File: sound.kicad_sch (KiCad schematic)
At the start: 19 parts, among them IC1 MAX4466EXK+T, U202 LSM6DS3

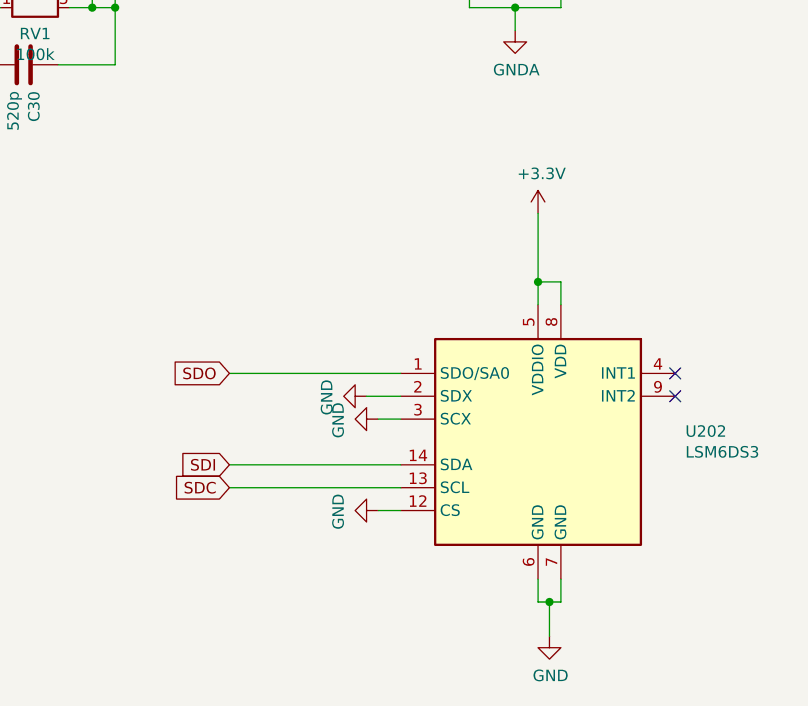
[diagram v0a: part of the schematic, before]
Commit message: Updated PCB after DRC. Updated Connector lib.
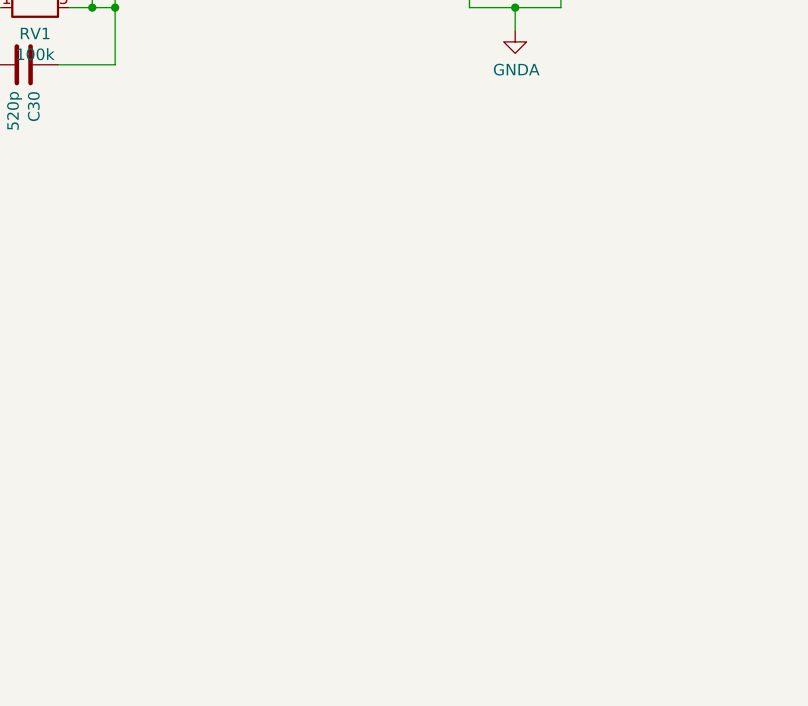
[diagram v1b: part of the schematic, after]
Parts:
- removed U202: LSM6DS3, Package_LGA:LGA-14_3x2.5mm_P0.5mm_LayoutBorder3x4y, symbol Sensor_Motion:LSM6DS3
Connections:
- no-connect marks 2 -> 0
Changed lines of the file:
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@@
   (junction (at 170.18 52.07) (diameter 0) (color 0 0 0 0)
   )
-  (junction (at 167.64 97.79) (diameter 0) (color 0 0 0 0)
-  )
   (junction (at 48.26 52.07) (diameter 0) (color 0 0 0 0)
   )
@@
   (junction (at 48.26 39.37) (diameter 0) (color 0 0 0 0)
   )
-  (junction (at 168.91 133.35) (diameter 0) (color 0 0 0 0)
-  )
   (junction (at 160.02 52.07) (diameter 0) (color 0 0 0 0)
   )
@@
   (junction (at 78.74 52.07) (diameter 0) (color 0 0 0 0)
   )
-  (no_connect (at 182.88 107.95))
-  (no_connect (at 182.88 110.49))
   (wire (pts (xy 111.76 63.5) (xy 118.11 63.5))
     (stroke (width 0) (type default) (color 0 0 0 0))
@@
     (stroke (width 0) (type default) (color 0 0 0 0))
   )
-  (wire (pts (xy 167.64 133.35) (xy 167.64 130.81))
-    (stroke (width 0) (type default) (color 0 0 0 0))
-  )
   (wire (pts (xy 88.9 57.15) (xy 88.9 67.31))
     (stroke (width 0) (type default) (color 0 0 0 0))
@@
     (stroke (width 0) (type default) (color 0 0 0 0))
   )
-  (wire (pts (xy 149.86 113.03) (xy 152.4 113.03))
-    (stroke (width 0) (type default) (color 0 0 0 0))
-  )
   (wire (pts (xy 120.65 52.07) (xy 120.65 67.31))
     (stroke (width 0) (type default) (color 0 0 0 0))
@@
     (stroke (width 0) (type default) (color 0 0 0 0))
   )
-  (wire (pts (xy 168.91 133.35) (xy 167.64 133.35))
-    (stroke (width 0) (type default) (color 0 0 0 0))
-  )
-  (wire (pts (xy 168.91 137.16) (xy 168.91 133.35))
-    (stroke (width 0) (type default) (color 0 0 0 0))
-  )
   (wire (pts (xy 78.74 50.8) (xy 78.74 52.07))
     (stroke (width 0) (type default) (color 0 0 0 0))
   )
-  (wire (pts (xy 133.35 120.65) (xy 152.4 120.65))
-    (stroke (width 0) (type default) (color 0 0 0 0))
-  )
   (wire (pts (xy 48.26 52.07) (xy 64.77 52.07))
     (stroke (width 0) (type default) (color 0 0 0 0))
@@
     (stroke (width 0) (type default) (color 0 0 0 0))
   )
-  (wire (pts (xy 170.18 97.79) (xy 167.64 97.79))
-    (stroke (width 0) (type default) (color 0 0 0 0))
-  )
   (wire (pts (xy 88.9 73.66) (xy 88.9 77.47))
     (stroke (width 0) (type default) (color 0 0 0 0))
@@
     (stroke (width 0) (type default) (color 0 0 0 0))
   )
-  (wire (pts (xy 170.18 100.33) (xy 170.18 97.79))
-    (stroke (width 0) (type default) (color 0 0 0 0))
-  )
-  (wire (pts (xy 167.64 90.17) (xy 167.64 97.79))
-    (stroke (width 0) (type default) (color 0 0 0 0))
-  )
   (wire (pts (xy 139.7 60.96) (xy 147.32 60.96))
     (stroke (width 0) (type default) (color 0 0 0 0))
@@
     (stroke (width 0) (type default) (color 0 0 0 0))
   )
-  (wire (pts (xy 149.86 123.19) (xy 152.4 123.19))
-    (stroke (width 0) (type default) (color 0 0 0 0))
-  )
   (wire (pts (xy 170.18 55.88) (xy 170.18 52.07))
     (stroke (width 0) (type default) (color 0 0 0 0))
@@
     (stroke (width 0) (type default) (color 0 0 0 0))
   )
-  (wire (pts (xy 167.64 97.79) (xy 167.64 100.33))
-    (stroke (width 0) (type default) (color 0 0 0 0))
-  )
   (wire (pts (xy 114.3 73.66) (xy 120.65 73.66))
     (stroke (width 0) (type default) (color 0 0 0 0))
@@
     (stroke (width 0) (type default) (color 0 0 0 0))
   )
-  (wire (pts (xy 133.35 118.11) (xy 152.4 118.11))
-    (stroke (width 0) (type default) (color 0 0 0 0))
-  )
   (wire (pts (xy 78.74 43.18) (xy 78.74 40.64))
     (stroke (width 0) (type default) (color 0 0 0 0))
@@
     (stroke (width 0) (type default) (color 0 0 0 0))
   )
-  (wire (pts (xy 170.18 133.35) (xy 168.91 133.35))
-    (stroke (width 0) (type default) (color 0 0 0 0))
-  )
   (wire (pts (xy 165.1 69.85) (xy 165.1 67.31))
     (stroke (width 0) (type default) (color 0 0 0 0))
@@
     (stroke (width 0) (type default) (color 0 0 0 0))
   )
-  (wire (pts (xy 148.59 110.49) (xy 152.4 110.49))
-    (stroke (width 0) (type default) (color 0 0 0 0))
-  )
   (wire (pts (xy 72.39 52.07) (xy 78.74 52.07))
     (stroke (width 0) (type default) (color 0 0 0 0))
@@
     (stroke (width 0) (type default) (color 0 0 0 0))
   )
-  (wire (pts (xy 133.35 107.95) (xy 152.4 107.95))
-    (stroke (width 0) (type default) (color 0 0 0 0))
-  )
   (wire (pts (xy 88.9 97.79) (xy 88.9 95.25))
     (stroke (width 0) (type default) (color 0 0 0 0))
@@
   )
   (wire (pts (xy 170.18 67.31) (xy 170.18 63.5))
-    (stroke (width 0) (type default) (color 0 0 0 0))
-  )
-  (wire (pts (xy 170.18 130.81) (xy 170.18 133.35))
     (stroke (width 0) (type default) (color 0 0 0 0))
   )
@@
   (label "AUDIO_AMP-" (at 88.9 71.12 0)
     (effects (font (size 1.27 1.27)) (justify left bottom))
-  )
-  (global_label "SDO" (shape input) (at 133.35 107.95 180) (fields_autoplaced)
-    (effects (font (size 1.27 1.27)) (justify right))
-    (property "Intersheet References" "${INTERSHEET_REFS}" (id 0) (at 0 0 0)
-      (effects (font (size 1.27 1.27)) hide)
-    )
-  )
-  (global_label "SDI" (shape input) (at 133.35 118.11 180) (fields_autoplaced)
-    (effects (font (size 1.27 1.27)) (justify right))
-    (property "Intersheet References" "${INTERSHEET_REFS}" (id 0) (at 0 0 0)
-      (effects (font (size 1.27 1.27)) hide)
-    )
-  )
-  (global_label "SDC" (shape input) (at 133.35 120.65 180) (fields_autoplaced)
-    (effects (font (size 1.27 1.27)) (justify right))
-    (property "Intersheet References" "${INTERSHEET_REFS}" (id 0) (at 0 0 0)
-      (effects (font (size 1.27 1.27)) hide)
-    )
   )
   (global_label "AUDIO_OUT" (shape input) (at 180.34 50.8 0) (fields_autoplaced)
@@
       (effects (font (size 1.27 1.27)) hide)
     )
-    (pin "1")
-  )
-  (symbol (lib_id "Sensor_Motion:LSM6DS3") (at 167.64 115.57 0) (unit 1)
-    (in_bom yes) (on_board yes)
-    (property "Reference" "U202" (id 0) (at 183.9976 114.4016 0)
-      (effects (font (size 1.27 1.27)) (justify left))
-    )
-    (property "Value" "LSM6DS3" (id 1) (at 183.9976 116.713 0)
-      (effects (font (size 1.27 1.27)) (justify left))
-    )
-    (property "Footprint" "Package_LGA:LGA-14_3x2.5mm_P0.5mm_LayoutBorder3x4y" (id 2) (at 157.48 133.35 0)
-      (effects (font (size 1.27 1.27)) (justify left) hide)
-    )
-    (property "Datasheet" "www.st.com/resource/en/datasheet/lsm6ds3.pdf" (id 3) (at 170.18 132.08 0)
-      (effects (font (size 1.27 1.27)) hide)
-    )
-    (pin "1")
-    (pin "10")
-    (pin "11")
-    (pin "12")
-    (pin "13")
-    (pin "14")
-    (pin "2")
-    (pin "3")
-    (pin "4")
-    (pin "5")
-    (pin "6")
-    (pin "7")
-    (pin "8")
-    (pin "9")
-  )
-  (symbol (lib_id "power:GND") (at 168.91 137.16 0) (unit 1)
-    (in_bom yes) (on_board yes)
-    (property "Reference" "#PWR0124" (id 0) (at 168.91 143.51 0)
-      (effects (font (size 1.27 1.27)) hide)
-    )
-    (property "Value" "GND" (id 1) (at 169.037 141.5542 0))
-    (property "Footprint" "" (id 2) (at 168.91 137.16 0)
-      (effects (font (size 1.27 1.27)) hide)
-    )
-    (property "Datasheet" "" (id 3) (at 168.91 137.16 0)
-      (effects (font (size 1.27 1.27)) hide)
-    )
-    (pin "1")
-  )
-  (symbol (lib_id "power:+3.3V") (at 167.64 90.17 0) (unit 1)
-    (in_bom yes) (on_board yes)
-    (property "Reference" "#PWR0125" (id 0) (at 167.64 93.98 0)
-      (effects (font (size 1.27 1.27)) hide)
-    )
-    (property "Value" "+3.3V" (id 1) (at 168.021 85.7758 0))
-    (property "Footprint" "" (id 2) (at 167.64 90.17 0)
-      (effects (font (size 1.27 1.27)) hide)
-    )
-    (property "Datasheet" "" (id 3) (at 167.64 90.17 0)
-      (effects (font (size 1.27 1.27)) hide)
-    )
-    (pin "1")
-  )
-  (symbol (lib_id "power:GND") (at 149.86 113.03 270) (unit 1)
-    (in_bom yes) (on_board yes)
-    (property "Reference" "#PWR0126" (id 0) (at 143.51 113.03 0)
-      (effects (font (size 1.27 1.27)) hide)
-    )
-    (property "Value" "GND" (id 1) (at 145.4658 113.157 0))
-    (property "Footprint" "" (id 2) (at 149.86 113.03 0)
-      (effects (font (size 1.27 1.27)) hide)
-    )
-    (property "Datasheet" "" (id 3) (at 149.86 113.03 0)
-      (effects (font (size 1.27 1.27)) hide)
-    )
-    (pin "1")
-  )
-  (symbol (lib_id "power:GND") (at 148.59 110.49 270) (unit 1)
-    (in_bom yes) (on_board yes)
-    (property "Reference" "#PWR0127" (id 0) (at 142.24 110.49 0)
-      (effects (font (size 1.27 1.27)) hide)
-    )
-    (property "Value" "GND" (id 1) (at 144.1958 110.617 0))
-    (property "Footprint" "" (id 2) (at 148.59 110.49 0)
-      (effects (font (size 1.27 1.27)) hide)
-    )
-    (property "Datasheet" "" (id 3) (at 148.59 110.49 0)
-      (effects (font (size 1.27 1.27)) hide)
-    )
-    (pin "1")
-  )
-  (symbol (lib_id "power:GND") (at 149.86 123.19 270) (unit 1)
-    (in_bom yes) (on_board yes)
-    (property "Reference" "#PWR0128" (id 0) (at 143.51 123.19 0)
-      (effects (font (size 1.27 1.27)) hide)
-    )
-    (property "Value" "GND" (id 1) (at 145.4658 123.317 0))
-    (property "Footprint" "" (id 2) (at 149.86 123.19 0)
-      (effects (font (size 1.27 1.27)) hide)
-    )
-    (property "Datasheet" "" (id 3) (at 149.86 123.19 0)
-      (effects (font (size 1.27 1.27)) hide)
-    )

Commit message: Updated power section. Updated all possible footprints to be "hand solder" version. Updated Symbol lib.
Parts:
- C27, C28, C29, C30, C310, C311: footprint Capacitor_SMD:C_0603_1608Metric -> Capacitor_SMD:C_0603_1608Metric_Pad1.08x0.95mm_HandSolder
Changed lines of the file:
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@@
       (effects (font (size 1.27 1.27)) (justify left))
     )
-    (property "Footprint" "Capacitor_SMD:C_0603_1608Metric" (id 2) (at 33.9852 45.72 0)
+    (property "Footprint" "Capacitor_SMD:C_0603_1608Metric_Pad1.08x0.95mm_HandSolder" (id 2) (at 33.9852 45.72 0)
       (effects (font (size 1.27 1.27)) hide)
     )
@@
       (effects (font (size 1.27 1.27)) (justify left))
     )
-    (property "Footprint" "Capacitor_SMD:C_0603_1608Metric" (id 2) (at 72.39 51.1048 0)
+    (property "Footprint" "Capacitor_SMD:C_0603_1608Metric_Pad1.08x0.95mm_HandSolder" (id 2) (at 72.39 51.1048 0)
       (effects (font (size 1.27 1.27)) hide)
     )
@@
       (effects (font (size 1.27 1.27)) (justify left))
     )
-    (property "Footprint" "Capacitor_SMD:C_0603_1608Metric" (id 2) (at 87.9348 87.63 0)
+    (property "Footprint" "Capacitor_SMD:C_0603_1608Metric_Pad1.08x0.95mm_HandSolder" (id 2) (at 87.9348 87.63 0)
       (effects (font (size 1.27 1.27)) hide)
     )
@@
       (effects (font (size 1.27 1.27)) (justify left))
     )
-    (property "Footprint" "Capacitor_SMD:C_0603_1608Metric" (id 2) (at 106.68 74.6252 0)
+    (property "Footprint" "Capacitor_SMD:C_0603_1608Metric_Pad1.08x0.95mm_HandSolder" (id 2) (at 106.68 74.6252 0)
       (effects (font (size 1.27 1.27)) hide)
     )
@@
       (effects (font (size 1.27 1.27)) (justify left))
     )
-    (property "Footprint" "Capacitor_SMD:C_0603_1608Metric" (id 2) (at 159.0548 55.88 0)
+    (property "Footprint" "Capacitor_SMD:C_0603_1608Metric_Pad1.08x0.95mm_HandSolder" (id 2) (at 159.0548 55.88 0)
       (effects (font (size 1.27 1.27)) hide)
     )
@@
       (effects (font (size 1.27 1.27)) (justify left))
     )
-    (property "Footprint" "Capacitor_SMD:C_0603_1608Metric" (id 2) (at 169.2148 55.88 0)
-      (effects (font (size 1.27 1.27)) hide)
-    )
+    (property "Footprint" "Capacitor_SMD:C_0603_1608Metric_Pad1.08x0.95mm_HandSolder" (id 2) (at 169.2148 55.88 0)
+      (effects (font (size 1.27 1.27)) hide)
+    )
